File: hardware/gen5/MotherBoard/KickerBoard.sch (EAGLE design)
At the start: 154 parts, among them U1 SAM3S4B

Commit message: All parts are not placed on the main board... not to do the traces
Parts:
- renumbered 12VGND_TEST to 12VGND, 12V_TEST to 12V, 3.3V_TEST to 3.3V, BATSENSE_TEST to BAT, GND_TEST to GND
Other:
- moved on the sheet: KICK
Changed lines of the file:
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@@
 <part name="DONE_TEST" library="gen3" deviceset="TEST_PT" device=""/>
 <part name="GATE_TEST" library="gen3" deviceset="TEST_PT" device=""/>
-<part name="GND_TEST" library="gen3" deviceset="TEST_PT" device=""/>
-<part name="12VGND_TEST" library="gen3" deviceset="TEST_PT" device=""/>
+<part name="GND" library="gen3" deviceset="TEST_PT" device=""/>
+<part name="12VGND" library="gen3" deviceset="TEST_PT" device=""/>
 <part name="C6" library="rcl" deviceset="CPOL-US" device="E10-35" value="1500uF"/>
 <part name="C14" library="rcl" deviceset="CPOL-US" device="E10-35" value="1500uF"/>
@@
 <part name="C8" library="SparkFun-Capacitors" deviceset="CAP" device="0805" value="1uF"/>
 <part name="ON/OFF" library="gen3" deviceset="SPDT-SWITCH" device=""/>
-<part name="3.3V_TEST" library="gen3" deviceset="TEST_PT" device=""/>
+<part name="3.3V" library="gen3" deviceset="TEST_PT" device=""/>
 <part name="3.3REG1" library="gen3" deviceset="3.3REG1A" device="REG"/>
 <part name="C9" library="SparkFun-Capacitors" deviceset="CAP" device="0805" value=".01uF"/>
@@
 <part name="R17" library="SparkFun-Passives" deviceset="RESISTOR" device="0805-RES" value="80k"/>
 <part name="R18" library="SparkFun-Passives" deviceset="RESISTOR" device="0805-RES" value="20k"/>
-<part name="12V_TEST" library="gen3" deviceset="TEST_PT" device=""/>
+<part name="12V" library="gen3" deviceset="TEST_PT" device=""/>
 <part name="BATCLAMP2" library="gen3" deviceset="DIODE-ZENER" device="DO214AC" value="DIODE-ZENERDO214AC"/>
 <part name="DRIB_TRAN" library="gen3" deviceset="N-MOSFET" device="DPAK"/>
 <part name="DRIB" library="gen3" deviceset="JST-2" device="2MM"/>
 <part name="DRIB_TEST" library="gen3" deviceset="TEST_PT" device=""/>
-<part name="BATSENSE_TEST" library="gen3" deviceset="TEST_PT" device=""/>
+<part name="BAT" library="gen3" deviceset="TEST_PT" device=""/>
 <part name="R19" library="SparkFun-Passives" deviceset="RESISTOR" device="0805-RES" value="20"/>
 <part name="C12" library="SparkFun-Capacitors" deviceset="CAP" device="0805" value="4.7uF"/>
@@
 <instance part="KICK_FLY" gate="G$1" x="480.06" y="332.74" rot="R90"/>
 <instance part="ANDS" gate="G$1" x="365.76" y="302.26"/>
-<instance part="KICK" gate="G$1" x="490.22" y="332.74"/>
+<instance part="KICK" gate="G$1" x="490.22" y="335.28"/>
 <instance part="KICK_Q1" gate="G$1" x="480.06" y="254"/>
 <instance part="CHIP_FLY" gate="G$1" x="480.06" y="274.32" rot="R90"/>
@@
 <instance part="DONE_TEST" gate="G$1" x="617.22" y="320.04"/>
 <instance part="GATE_TEST" gate="G$1" x="688.34" y="317.5"/>
-<instance part="GND_TEST" gate="G$1" x="655.32" y="254"/>
-<instance part="12VGND_TEST" gate="G$1" x="754.38" y="248.92" rot="R270"/>
+<instance part="GND" gate="G$1" x="655.32" y="254"/>
+<instance part="12VGND" gate="G$1" x="754.38" y="248.92" rot="R270"/>
 <instance part="C6" gate="G$1" x="665.48" y="358.14"/>
 <instance part="C14" gate="G$1" x="678.18" y="358.14"/>
@@
 <instance part="C8" gate="G$1" x="449.58" y="347.98"/>
 <instance part="ON/OFF" gate="G$1" x="383.54" y="360.68"/>
-<instance part="3.3V_TEST" gate="G$1" x="441.96" y="358.14"/>
+<instance part="3.3V" gate="G$1" x="441.96" y="358.14"/>
 <instance part="3.3REG1" gate="G$1" x="419.1" y="347.98" rot="MR270"/>
 <instance part="C9" gate="G$1" x="462.28" y="347.98"/>
@@
 <instance part="R17" gate="G$1" x="556.26" y="284.48" rot="R90"/>
 <instance part="R18" gate="G$1" x="556.26" y="269.24" rot="R90"/>
-<instance part="12V_TEST" gate="G$1" x="403.86" y="358.14"/>
+<instance part="12V" gate="G$1" x="403.86" y="358.14"/>
 <instance part="BATCLAMP2" gate="G$1" x="543.56" y="271.78" smashed="yes" rot="R90">
 <attribute name="NAME" x="540.5374" y="261.62" size="1.778" layer="95" rot="R90"/>
@@
 <instance part="DRIB" gate="G$1" x="332.74" y="365.76"/>
 <instance part="DRIB_TEST" gate="G$1" x="289.56" y="353.06"/>
-<instance part="BATSENSE_TEST" gate="G$1" x="548.64" y="279.4" smashed="yes">
+<instance part="BAT" gate="G$1" x="548.64" y="279.4" smashed="yes">
 <attribute name="NAME" x="544.83" y="274.32" size="1.778" layer="95"/>
 </instance>
@@
 <pinref part="C19" gate="G$1" pin="2"/>
 <pinref part="CHARGE_U" gate="G$1" pin="GND"/>
-<pinref part="GND_TEST" gate="G$1" pin="P$1"/>
+<pinref part="GND" gate="G$1" pin="P$1"/>
 <wire x1="655.32" y1="251.46" x2="655.32" y2="248.92" width="0.1524" layer="91"/>
 <junction x="655.32" y="248.92"/>
@@
 <pinref part="C9" gate="G$1" pin="1"/>
 <wire x1="462.28" y1="355.6" x2="462.28" y2="353.06" width="0.1524" layer="91"/>
-<pinref part="3.3V_TEST" gate="G$1" pin="P$1"/>
+<pinref part="3.3V" gate="G$1" pin="P$1"/>
 <wire x1="449.58" y1="355.6" x2="441.96" y2="355.6" width="0.1524" layer="91"/>
 <junction x="449.58" y="355.6"/>
@@
 <wire x1="716.28" y1="248.92" x2="716.28" y2="241.3" width="0.1524" layer="91"/>
 <junction x="716.28" y="248.92"/>
-<pinref part="12VGND_TEST" gate="G$1" pin="P$1"/>
+<pinref part="12VGND" gate="G$1" pin="P$1"/>
 <junction x="751.84" y="248.92"/>
 </segment>
@@
 </segment>
 <segment>
-<wire x1="485.14" y1="337.82" x2="485.14" y2="335.28" width="0.1524" layer="91"/>
 <pinref part="KICK_FLY" gate="G$1" pin="C"/>
 <wire x1="480.06" y1="335.28" x2="480.06" y2="337.82" width="0.1524" layer="91"/>
@@
 <pinref part="ON/OFF" gate="G$1" pin="P2"/>
 <wire x1="393.7" y1="355.6" x2="401.32" y2="355.6" width="0.1524" layer="91"/>
-<pinref part="12V_TEST" gate="G$1" pin="P$1"/>
+<pinref part="12V" gate="G$1" pin="P$1"/>
 <wire x1="401.32" y1="355.6" x2="403.86" y2="355.6" width="0.1524" layer="91"/>
 <wire x1="403.86" y1="355.6" x2="414.02" y2="355.6" width="0.1524" layer="91"/>
@@
 <segment>
 <pinref part="KICK" gate="G$1" pin="P$2"/>
-<wire x1="485.14" y1="325.12" x2="485.14" y2="330.2" width="0.1524" layer="91"/>
+<wire x1="485.14" y1="325.12" x2="485.14" y2="332.74" width="0.1524" layer="91"/>
 <pinref part="KICK_FLY" gate="G$1" pin="A"/>
 <wire x1="480.06" y1="330.2" x2="480.06" y2="325.12" width="0.1524" layer="91"/>
@@
 <wire x1="543.56" y1="276.86" x2="533.4" y2="276.86" width="0.1524" layer="91"/>
 <wire x1="543.56" y1="274.32" x2="543.56" y2="276.86" width="0.1524" layer="91"/>
-<pinref part="BATSENSE_TEST" gate="G$1" pin="P$1"/>
+<pinref part="BAT" gate="G$1" pin="P$1"/>
 <junction x="548.64" y="276.86"/>
 <junction x="556.26" y="276.86"/>

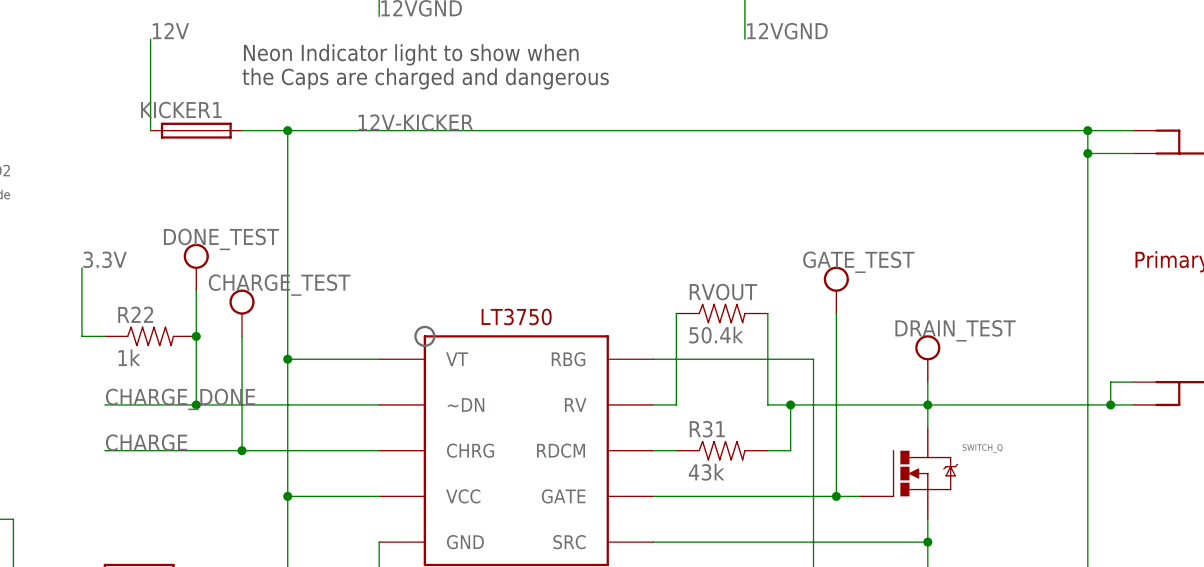
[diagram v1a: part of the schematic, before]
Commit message: Began adding traces to the Motherboard.
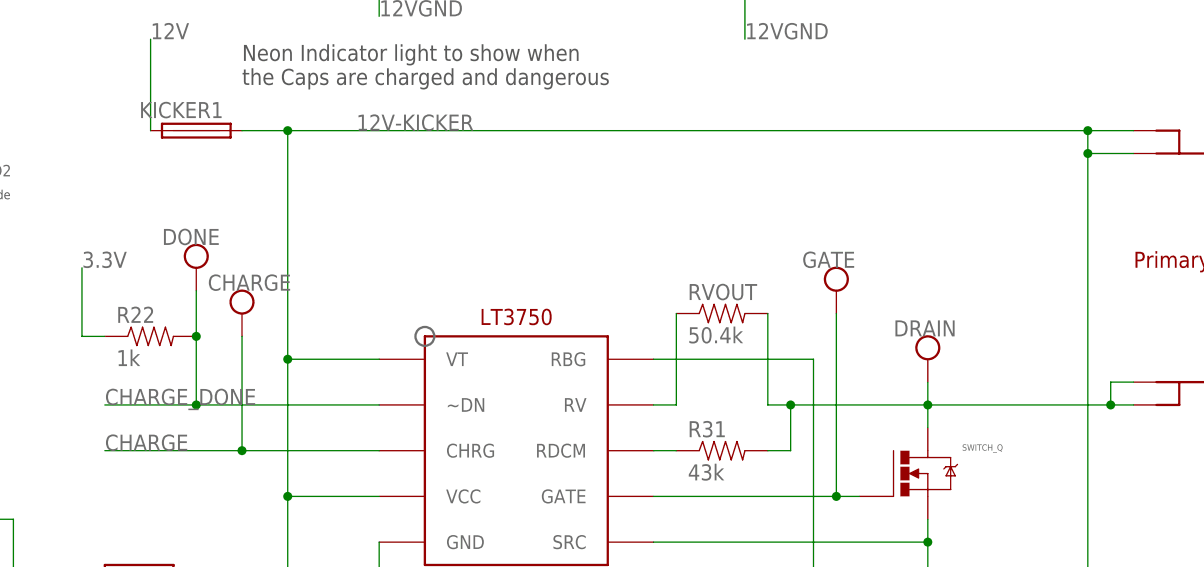
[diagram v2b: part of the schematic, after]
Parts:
- renumbered CHARGE_TEST to CHARGE, DONE_TEST to DONE, DRAIN_TEST to DRAIN, GATE_TEST to GATE
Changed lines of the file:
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@@
 <part name="SWITCH_Q" library="gen3" deviceset="N-MOSFET" device="DPAK"/>
 <part name="U$3" library="gen3" deviceset="32052-TRANSFORMER" device=""/>
-<part name="DRAIN_TEST" library="gen3" deviceset="TEST_PT" device=""/>
-<part name="CHARGE_TEST" library="gen3" deviceset="TEST_PT" device=""/>
-<part name="DONE_TEST" library="gen3" deviceset="TEST_PT" device=""/>
-<part name="GATE_TEST" library="gen3" deviceset="TEST_PT" device=""/>
+<part name="DRAIN" library="gen3" deviceset="TEST_PT" device=""/>
+<part name="CHARGE" library="gen3" deviceset="TEST_PT" device=""/>
+<part name="DONE" library="gen3" deviceset="TEST_PT" device=""/>
+<part name="GATE" library="gen3" deviceset="TEST_PT" device=""/>
 <part name="GND" library="gen3" deviceset="TEST_PT" device=""/>
 <part name="12VGND" library="gen3" deviceset="TEST_PT" device=""/>
@@
 <instance part="SWITCH_Q" gate="G$1" x="695.96" y="297.18"/>
 <instance part="U$3" gate="G$1" x="734.06" y="320.04"/>
-<instance part="DRAIN_TEST" gate="G$1" x="698.5" y="309.88"/>
-<instance part="CHARGE_TEST" gate="G$1" x="622.3" y="314.96"/>
-<instance part="DONE_TEST" gate="G$1" x="617.22" y="320.04"/>
-<instance part="GATE_TEST" gate="G$1" x="688.34" y="317.5"/>
+<instance part="DRAIN" gate="G$1" x="698.5" y="309.88"/>
+<instance part="CHARGE" gate="G$1" x="622.3" y="314.96"/>
+<instance part="DONE" gate="G$1" x="617.22" y="320.04"/>
+<instance part="GATE" gate="G$1" x="688.34" y="317.5"/>
 <instance part="GND" gate="G$1" x="655.32" y="254"/>
 <instance part="12VGND" gate="G$1" x="754.38" y="248.92" rot="R270"/>
@@
 <pinref part="U$3" gate="G$1" pin="P$6"/>
 <pinref part="U$3" gate="G$1" pin="P$7"/>
-<pinref part="DRAIN_TEST" gate="G$1" pin="P$1"/>
+<pinref part="DRAIN" gate="G$1" pin="P$1"/>
 <wire x1="698.5" y1="307.34" x2="698.5" y2="304.8" width="0.1524" layer="91"/>
 </segment>
@@
 <pinref part="CHARGE_U" gate="G$1" pin="GATE"/>
 <pinref part="SWITCH_Q" gate="G$1" pin="G"/>
-<pinref part="GATE_TEST" gate="G$1" pin="P$1"/>
+<pinref part="GATE" gate="G$1" pin="P$1"/>
 <wire x1="688.34" y1="294.64" x2="690.88" y2="294.64" width="0.1524" layer="91"/>
 <wire x1="688.34" y1="314.96" x2="688.34" y2="294.64" width="0.1524" layer="91"/>
@@
 <pinref part="CHARGE_U" gate="G$1" pin="CHRG"/>
 <label x="607.06" y="299.72" size="1.778" layer="95"/>
-<pinref part="CHARGE_TEST" gate="G$1" pin="P$1"/>
+<pinref part="CHARGE" gate="G$1" pin="P$1"/>
 <wire x1="622.3" y1="299.72" x2="607.06" y2="299.72" width="0.1524" layer="91"/>
 <wire x1="622.3" y1="312.42" x2="622.3" y2="299.72" width="0.1524" layer="91"/>
@@
 <label x="607.06" y="304.8" size="1.778" layer="95"/>
 <pinref part="CHARGE_U" gate="G$1" pin="~DN"/>
-<pinref part="DONE_TEST" gate="G$1" pin="P$1"/>
+<pinref part="DONE" gate="G$1" pin="P$1"/>
 <wire x1="617.22" y1="304.8" x2="607.06" y2="304.8" width="0.1524" layer="91"/>
 <wire x1="617.22" y1="317.5" x2="617.22" y2="312.42" width="0.1524" layer="91"/>

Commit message: More motherboard work!
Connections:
- removed net N$39: MOTOR2.15, MOTOR2.16, MOTOR2.17, MOTOR2.18, U$8.P$5, U$8.P$6
- net 12VGND: now also MOTOR1.22, MOTOR1.33, MOTOR1.34, MOTOR2.15, MOTOR2.16, MOTOR2.17, MOTOR2.18, MOTOR2.22, MOTOR2.33, MOTOR2.34, MOTOR3.22, MOTOR3.33, MOTOR3.34, MOTOR4.22, MOTOR4.33, MOTOR4.34, U$10.P$7, U$11.P$7, U$8.P$5, U$8.P$6, U$9.P$7
- net GND: no longer MOTOR1.22, MOTOR1.33, MOTOR1.34, MOTOR2.22, MOTOR2.33, MOTOR2.34, MOTOR3.22, MOTOR3.33, MOTOR3.34, MOTOR4.22, MOTOR4.33, MOTOR4.34, U$10.P$7, U$11.P$7, U$9.P$7
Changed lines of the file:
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@@
-</segment>
-<segment>
-<wire x1="281.94" y1="208.28" x2="297.18" y2="208.28" width="0.1524" layer="91"/>
-<label x="279.4" y="208.28" size="1.778" layer="95"/>
-<pinref part="MOTOR1" gate="G$1" pin="33"/>
-<junction x="297.18" y="208.28"/>
-<pinref part="MOTOR1" gate="G$1" pin="34"/>
-<wire x1="297.18" y1="208.28" x2="312.42" y2="208.28" width="0.1524" layer="91"/>
-</segment>
-<segment>
-<label x="299.72" y="134.62" size="1.778" layer="95"/>
-<pinref part="MOTOR2" gate="G$1" pin="34"/>
-<wire x1="322.58" y1="134.62" x2="335.28" y2="134.62" width="0.1524" layer="91"/>
-<wire x1="335.28" y1="134.62" x2="320.04" y2="134.62" width="0.1524" layer="91"/>
-<pinref part="MOTOR2" gate="G$1" pin="33"/>
-<junction x="320.04" y="134.62"/>
-<wire x1="320.04" y1="134.62" x2="304.8" y2="134.62" width="0.1524" layer="91"/>
-<junction x="335.28" y="134.62"/>
-</segment>
-<segment>
-<label x="378.46" y="134.62" size="1.778" layer="95"/>
-<pinref part="MOTOR3" gate="G$1" pin="34"/>
-<wire x1="383.54" y1="134.62" x2="398.78" y2="134.62" width="0.1524" layer="91"/>
-<pinref part="MOTOR3" gate="G$1" pin="33"/>
-<junction x="398.78" y="134.62"/>
-<wire x1="398.78" y1="134.62" x2="414.02" y2="134.62" width="0.1524" layer="91"/>
-<junction x="414.02" y="134.62"/>
-</segment>
-<segment>
-<label x="457.2" y="134.62" size="1.778" layer="95"/>
-<pinref part="MOTOR4" gate="G$1" pin="34"/>
-<wire x1="462.28" y1="134.62" x2="477.52" y2="134.62" width="0.1524" layer="91"/>
-<pinref part="MOTOR4" gate="G$1" pin="33"/>
-<junction x="477.52" y="134.62"/>
-<wire x1="477.52" y1="134.62" x2="492.76" y2="134.62" width="0.1524" layer="91"/>
-<junction x="492.76" y="134.62"/>
 </segment>
 <segment>
@@
 </segment>
 <segment>
-<pinref part="MOTOR1" gate="G$1" pin="30"/>
-<pinref part="JP4" gate="G$1" pin="2"/>
-<wire x1="332.74" y1="213.36" x2="312.42" y2="213.36" width="0.1524" layer="91"/>
-<label x="317.5" y="213.36" size="1.778" layer="95"/>
-</segment>
-<segment>
-<pinref part="MOTOR2" gate="G$1" pin="22"/>
-<wire x1="335.28" y1="149.86" x2="340.36" y2="149.86" width="0.1524" layer="91"/>
-<label x="337.82" y="149.86" size="1.778" layer="95"/>
-</segment>
-<segment>
 <pinref part="U$8" gate="G$1" pin="P$7"/>
 <wire x1="287.02" y1="154.94" x2="289.56" y2="157.48" width="0.1524" layer="91"/>
 <wire x1="289.56" y1="157.48" x2="292.1" y2="157.48" width="0.1524" layer="91"/>
 <label x="289.56" y="157.48" size="1.778" layer="95"/>
-</segment>
-<segment>
-<pinref part="U$11" gate="G$1" pin="P$7"/>
-<wire x1="276.86" y1="228.6" x2="279.4" y2="231.14" width="0.1524" layer="91"/>
-<label x="279.4" y="231.14" size="1.778" layer="95"/>
-</segment>
-<segment>
-<pinref part="MOTOR1" gate="G$1" pin="22"/>
-<wire x1="312.42" y1="223.52" x2="314.96" y2="223.52" width="0.1524" layer="91"/>
-<label x="314.96" y="223.52" size="1.778" layer="95"/>
-</segment>
-<segment>
-<pinref part="U$9" gate="G$1" pin="P$7"/>
-<wire x1="373.38" y1="154.94" x2="375.92" y2="157.48" width="0.1524" layer="91"/>
-<label x="375.92" y="157.48" size="1.778" layer="95"/>
-</segment>
-<segment>
-<pinref part="MOTOR3" gate="G$1" pin="22"/>
-<wire x1="414.02" y1="149.86" x2="421.64" y2="149.86" width="0.1524" layer="91"/>
-<label x="416.56" y="149.86" size="1.778" layer="95"/>
-</segment>
-<segment>
-<pinref part="U$10" gate="G$1" pin="P$7"/>
-<wire x1="454.66" y1="154.94" x2="457.2" y2="157.48" width="0.1524" layer="91"/>
-<label x="457.2" y="157.48" size="1.778" layer="95"/>
-</segment>
-<segment>
-<pinref part="MOTOR4" gate="G$1" pin="22"/>
-<wire x1="492.76" y1="149.86" x2="497.84" y2="149.86" width="0.1524" layer="91"/>
-<label x="492.76" y="149.86" size="1.778" layer="95"/>
 </segment>
 <segment>
@@
 <label x="330.2" y="327.66" size="1.778" layer="95"/>
 </segment>
+<segment>
+<pinref part="MOTOR1" gate="G$1" pin="30"/>
+<pinref part="JP4" gate="G$1" pin="2"/>
+<wire x1="332.74" y1="213.36" x2="312.42" y2="213.36" width="0.1524" layer="91"/>
+<label x="317.5" y="213.36" size="1.778" layer="95"/>
+</segment>
 </net>
 <net name="3.3V" class="0">
@@
 <wire x1="541.02" y1="309.88" x2="553.72" y2="309.88" width="0.1524" layer="91"/>
 <junction x="553.72" y="309.88"/>
+</segment>
+<segment>
+<pinref part="U$11" gate="G$1" pin="P$7"/>
+<wire x1="276.86" y1="228.6" x2="279.4" y2="231.14" width="0.1524" layer="91"/>
+<label x="279.4" y="231.14" size="1.778" layer="95"/>
+</segment>
+<segment>
+<pinref part="MOTOR1" gate="G$1" pin="22"/>
+<wire x1="312.42" y1="223.52" x2="314.96" y2="223.52" width="0.1524" layer="91"/>
+<label x="314.96" y="223.52" size="1.778" layer="95"/>
+</segment>
+<segment>
+<wire x1="281.94" y1="208.28" x2="297.18" y2="208.28" width="0.1524" layer="91"/>
+<label x="279.4" y="208.28" size="1.778" layer="95"/>
+<pinref part="MOTOR1" gate="G$1" pin="33"/>
+<junction x="297.18" y="208.28"/>
+<pinref part="MOTOR1" gate="G$1" pin="34"/>
+<wire x1="297.18" y1="208.28" x2="312.42" y2="208.28" width="0.1524" layer="91"/>
+</segment>
+<segment>
+<pinref part="U$8" gate="G$1" pin="P$6"/>
+<pinref part="U$8" gate="G$1" pin="P$5"/>
+<wire x1="287.02" y1="157.48" x2="287.02" y2="160.02" width="0.1524" layer="91"/>
+<wire x1="287.02" y1="160.02" x2="314.96" y2="160.02" width="0.1524" layer="91"/>
+<wire x1="314.96" y1="160.02" x2="317.5" y2="157.48" width="0.1524" layer="91"/>
+<pinref part="MOTOR2" gate="G$1" pin="15"/>
+<wire x1="317.5" y1="157.48" x2="320.04" y2="157.48" width="0.1524" layer="91"/>
+<pinref part="MOTOR2" gate="G$1" pin="17"/>
+<wire x1="320.04" y1="154.94" x2="320.04" y2="157.48" width="0.1524" layer="91"/>
+<pinref part="MOTOR2" gate="G$1" pin="16"/>
+<wire x1="320.04" y1="157.48" x2="335.28" y2="157.48" width="0.1524" layer="91"/>
+<pinref part="MOTOR2" gate="G$1" pin="18"/>
+<wire x1="335.28" y1="157.48" x2="335.28" y2="154.94" width="0.1524" layer="91"/>
+<junction x="320.04" y="157.48"/>
+<junction x="320.04" y="154.94"/>
+<junction x="335.28" y="157.48"/>
+<junction x="335.28" y="154.94"/>
+</segment>
+<segment>
+<label x="299.72" y="134.62" size="1.778" layer="95"/>
+<pinref part="MOTOR2" gate="G$1" pin="34"/>
+<wire x1="322.58" y1="134.62" x2="335.28" y2="134.62" width="0.1524" layer="91"/>
+<wire x1="335.28" y1="134.62" x2="320.04" y2="134.62" width="0.1524" layer="91"/>
+<pinref part="MOTOR2" gate="G$1" pin="33"/>
+<junction x="320.04" y="134.62"/>
+<wire x1="320.04" y1="134.62" x2="304.8" y2="134.62" width="0.1524" layer="91"/>
+<junction x="335.28" y="134.62"/>
+</segment>
+<segment>
+<pinref part="MOTOR2" gate="G$1" pin="22"/>
+<wire x1="335.28" y1="149.86" x2="340.36" y2="149.86" width="0.1524" layer="91"/>
+<label x="337.82" y="149.86" size="1.778" layer="95"/>
+</segment>
+<segment>
+<pinref part="U$9" gate="G$1" pin="P$7"/>
+<wire x1="373.38" y1="154.94" x2="375.92" y2="157.48" width="0.1524" layer="91"/>
+<label x="375.92" y="157.48" size="1.778" layer="95"/>
+</segment>
+<segment>
+<label x="378.46" y="134.62" size="1.778" layer="95"/>
+<pinref part="MOTOR3" gate="G$1" pin="34"/>
+<wire x1="383.54" y1="134.62" x2="398.78" y2="134.62" width="0.1524" layer="91"/>
+<pinref part="MOTOR3" gate="G$1" pin="33"/>
+<junction x="398.78" y="134.62"/>
+<wire x1="398.78" y1="134.62" x2="414.02" y2="134.62" width="0.1524" layer="91"/>
+<junction x="414.02" y="134.62"/>
+</segment>
+<segment>
+<pinref part="MOTOR3" gate="G$1" pin="22"/>
+<wire x1="414.02" y1="149.86" x2="421.64" y2="149.86" width="0.1524" layer="91"/>
+<label x="416.56" y="149.86" size="1.778" layer="95"/>
+</segment>
+<segment>
+<pinref part="U$10" gate="G$1" pin="P$7"/>
+<wire x1="454.66" y1="154.94" x2="457.2" y2="157.48" width="0.1524" layer="91"/>
+<label x="457.2" y="157.48" size="1.778" layer="95"/>
+</segment>
+<segment>
+<label x="457.2" y="134.62" size="1.778" layer="95"/>
+<pinref part="MOTOR4" gate="G$1" pin="34"/>
+<wire x1="462.28" y1="134.62" x2="477.52" y2="134.62" width="0.1524" layer="91"/>
+<pinref part="MOTOR4" gate="G$1" pin="33"/>
+<junction x="477.52" y="134.62"/>
+<wire x1="477.52" y1="134.62" x2="492.76" y2="134.62" width="0.1524" layer="91"/>
+<junction x="492.76" y="134.62"/>
+</segment>
+<segment>
+<pinref part="MOTOR4" gate="G$1" pin="22"/>
+<wire x1="492.76" y1="149.86" x2="497.84" y2="149.86" width="0.1524" layer="91"/>
+<label x="492.76" y="149.86" size="1.778" layer="95"/>
 </segment>
 </net>
@@
 </segment>
 </net>
-<net name="N$39" class="0">
-<segment>
-<pinref part="U$8" gate="G$1" pin="P$6"/>
-<pinref part="U$8" gate="G$1" pin="P$5"/>
-<wire x1="287.02" y1="157.48" x2="287.02" y2="160.02" width="0.1524" layer="91"/>
-<wire x1="287.02" y1="160.02" x2="314.96" y2="160.02" width="0.1524" layer="91"/>
-<wire x1="314.96" y1="160.02" x2="317.5" y2="157.48" width="0.1524" layer="91"/>
-<pinref part="MOTOR2" gate="G$1" pin="15"/>
-<wire x1="317.5" y1="157.48" x2="320.04" y2="157.48" width="0.1524" layer="91"/>
-<pinref part="MOTOR2" gate="G$1" pin="17"/>
-<wire x1="320.04" y1="154.94" x2="320.04" y2="157.48" width="0.1524" layer="91"/>
-<pinref part="MOTOR2" gate="G$1" pin="16"/>
-<wire x1="320.04" y1="157.48" x2="335.28" y2="157.48" width="0.1524" layer="91"/>
-<pinref part="MOTOR2" gate="G$1" pin="18"/>
-<wire x1="335.28" y1="157.48" x2="335.28" y2="154.94" width="0.1524" layer="91"/>
-<junction x="320.04" y="157.48"/>
-<junction x="320.04" y="154.94"/>
-<junction x="335.28" y="157.48"/>
-<junction x="335.28" y="154.94"/>
-</segment>
-</net>
